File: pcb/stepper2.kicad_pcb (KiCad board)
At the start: 2 copper layers, 92 x 138 mm, 52 parts, among them J1 DA15_Receptacle_MountingHoles, J10 Conn_01x07_Pin, J11 FAN, J2 DA15_Receptacle_MountingHoles, J3 DA15_Receptacle_MountingHoles, J4 DE15_Receptacle_HighDensity, J5 DE15_Receptacle_HighDensity, J6 DE15_Receptacle_HighDensity, J7 Conn_01x04_Pin, J8 Conn_01x05_Pin, J9 Conn_01x06_Pin, SW1 SW_Push, SW2 SW_Push, SW3 SW_Push, SW4 SW_Push, SW5 SW_Push, SW6 SW_Push, U1 AM26LS32ACN, U2 AM26LS32Ax, U3 AM26LS32ACN, U4 TMC2226_BIGTREETECH, U5 TMC2209_BIGTREETECH, U6 TMC2209_BIGTREETECH

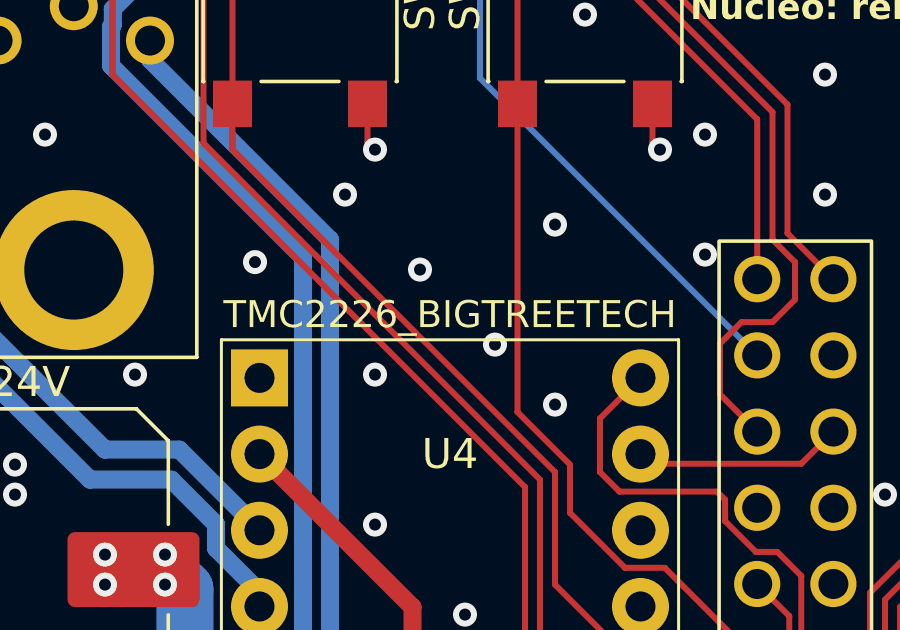
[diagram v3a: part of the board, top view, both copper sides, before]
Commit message: fixed mixed labeling for jog buttons; initial config of the NXT timers
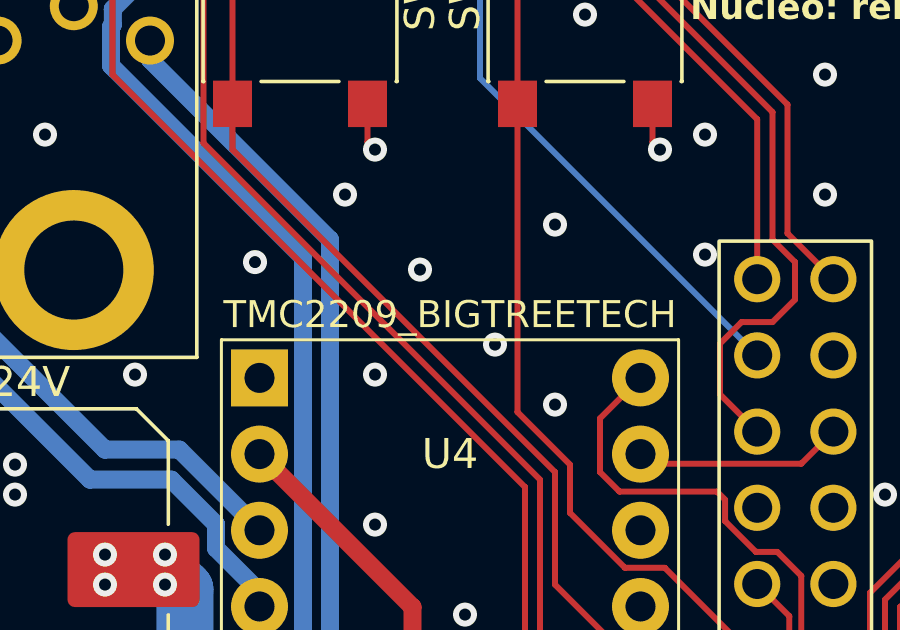
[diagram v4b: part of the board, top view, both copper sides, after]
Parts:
- U4: value TMC2226_BIGTREETECH -> TMC2209_BIGTREETECH
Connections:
- SW2 pad 1: UP2 -> DOWN3
- SW4 pad 1: DOWN1 -> DOWN2
- SW5 pad 1: DOWN2 -> UP2
- SW6 pad 1: DOWN3 -> DOWN1
- U10 pad B46: UP2 -> DOWN3
- U10 pad B50: DOWN3 -> DOWN1
- U10 pad B52: DOWN2 -> UP2
- U10 pad B54: DOWN1 -> DOWN2
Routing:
- net DOWN1: track 37.7 -> 56.2 mm
- net DOWN3: track 56.2 -> 41.5 mm
- net UP2: track 41.5 -> 31.9 mm, vias 0 -> 1
- net DOWN2: track 31.9 -> 37.7 mm, vias 1 -> 0

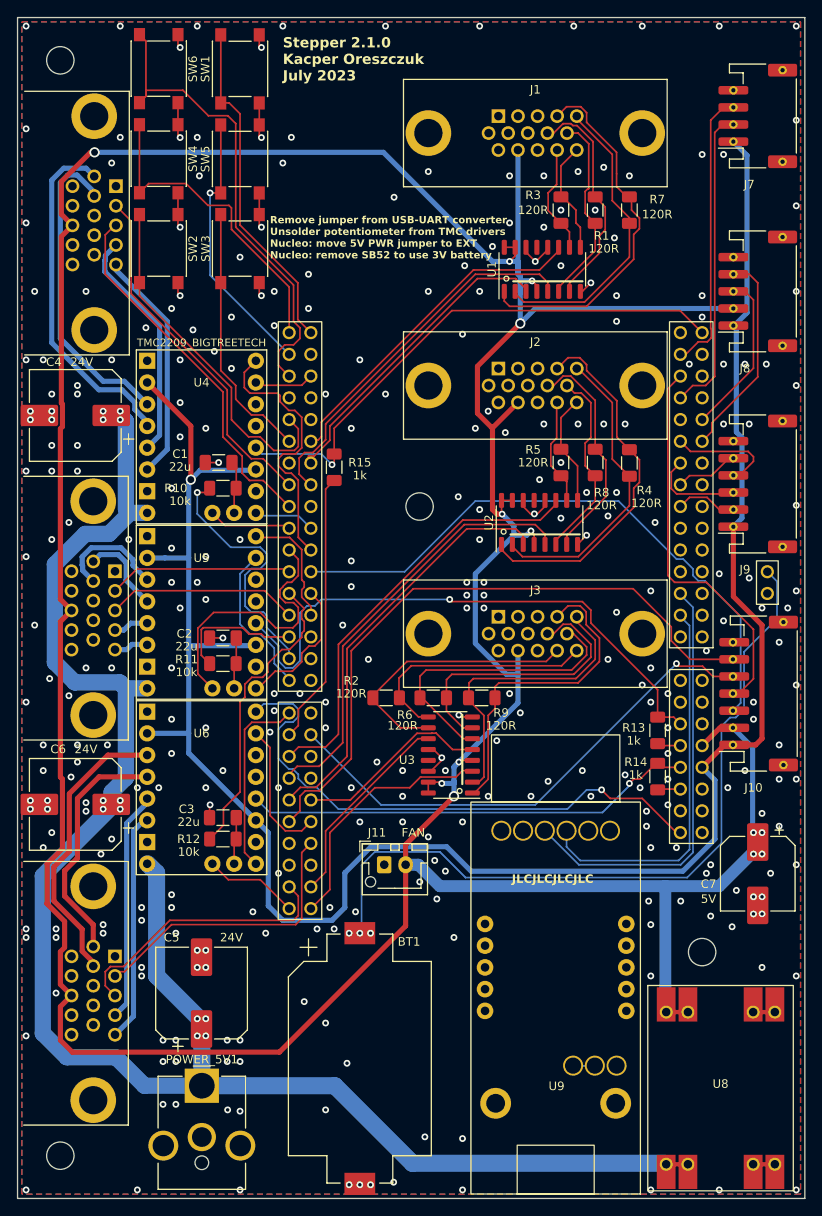
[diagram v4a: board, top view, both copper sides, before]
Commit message: PCB: NXT/DIR external output connectors and some polishing
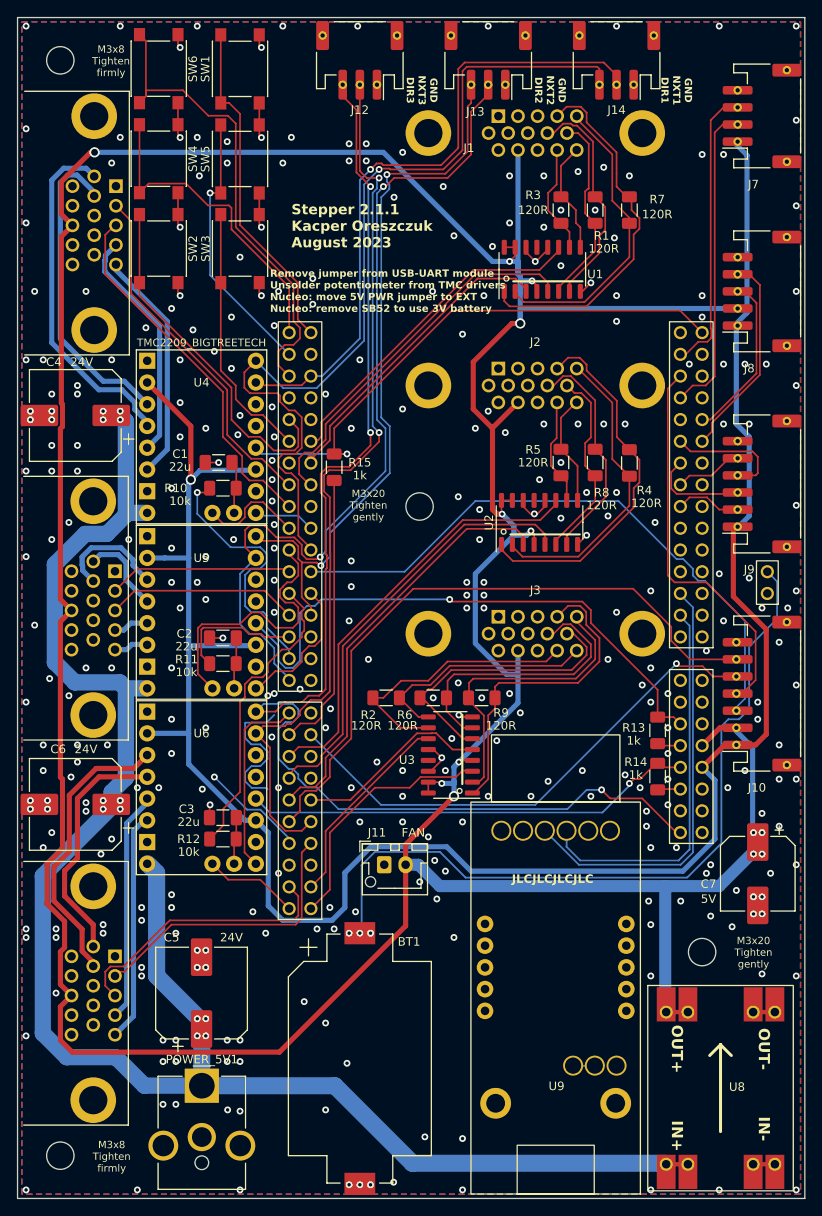
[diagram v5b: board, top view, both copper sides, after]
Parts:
- added J12: Conn_01x03_Pin, stepper2:JST_PH_S3B-PH-SM4-TB_1x03-1MP_P2.00mm_Horizontal, F.Cu at (40.0, 5.00)
- added J13: Conn_01x03_Pin, stepper2:JST_PH_S3B-PH-SM4-TB_1x03-1MP_P2.00mm_Horizontal, F.Cu at (55.0, 5.00)
- added J14: Conn_01x03_Pin, stepper2:JST_PH_S3B-PH-SM4-TB_1x03-1MP_P2.00mm_Horizontal, F.Cu at (70.0, 5.00)
- moved J7 0.50 mm to (87.0, 11.5)
- moved J8 0.50 mm to (87.0, 32.0)
- moved J9 0.50 mm to (87.0, 54.5)
- moved J10 0.40 mm to (87.0, 79.0)
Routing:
- net NXT3: track 16.2 -> 105.0 mm, vias 0 -> 2
- net DIR3: track 65.5 -> 151.2 mm, vias 1 -> 3
- net NXT2: track 18.2 -> 101.3 mm, vias 0 -> 2
- net DIR1: track 31.7 -> 106.9 mm, vias 0 -> 1
- net DIR2: track 14.4 -> 85.0 mm, vias 0 -> 2
- net NXT1: track 7.01 -> 76.2 mm, vias 0 -> 1
- net GND: track 43.4 -> 72.7 mm, vias 311 -> 332
- net DIAG1: track 9.71 -> 12.4 mm
- net +5V: track 458.4 -> 460.4 mm
- net EXTCOPI: track 12.9 -> 14.7 mm
- net +3V3: track 245.2 -> 246.8 mm
- net ENCB3+: track 35.0 -> 33.6 mm
- net ENCI3-: track 28.7 -> 27.3 mm
- net TMCUART1: track 63.8 -> 65.2 mm
- net TMCUARTTX1: track 31.9 -> 32.9 mm
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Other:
- board text added: "GND NXT1 DIR1"
- board text added: "GND NXT2 DIR2"
- board text added: "GND NXT3 DIR3"
- board text added: "M3x20 Tighten gently"
- board text added: "M3x8 Tighten firmly"
- board text added: "Remove jumper from USB-UART module Unsolder potentiometer from TMC drivers Nucleo: move 5V PWR jumper to EXT Nucleo: remove SB52 to use 3V battery"
- board text added: "Stepper 2.1.1 Kacper Oreszczuk August 2023"
- board text removed: "Remove jumper from USB-UART converter Unsolder potentiometer from TMC drivers Nucleo: move 5V PWR jumper to EXT Nucleo: remove SB52 to use 3V battery"
- board text removed: "Stepper 2.1.0 Kacper Oreszczuk July 2023"

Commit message: filtering capacitors for differential receivers; BOM and placement files for SMD elements
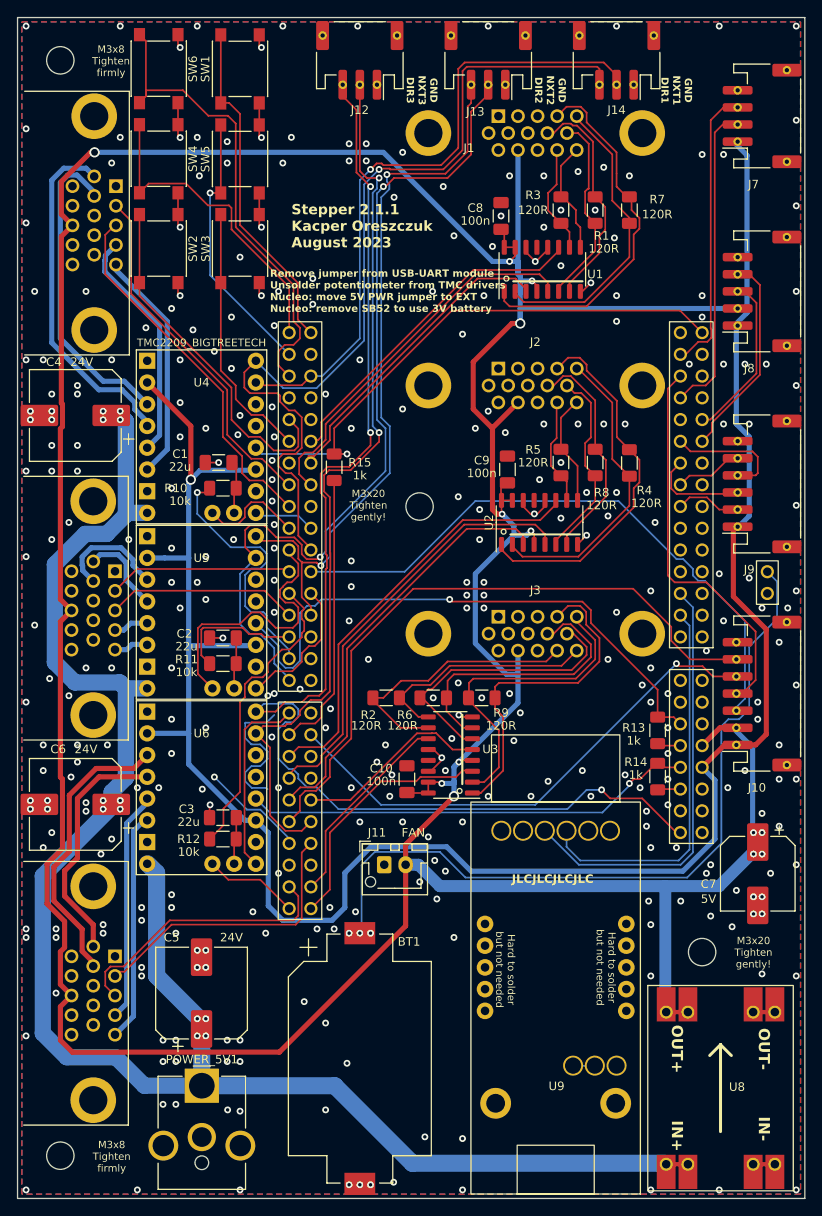
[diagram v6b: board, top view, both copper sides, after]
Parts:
- added C10: 100n, Capacitor_SMD:C_1206_3216Metric_Pad1.33x1.80mm_HandSolder, F.Cu at (45.5, 89.0)
- added C8: 100n, Capacitor_SMD:C_1206_3216Metric_Pad1.33x1.80mm_HandSolder, F.Cu at (56.5, 23.2)
- added C9: 100n, Capacitor_SMD:C_1206_3216Metric_Pad1.33x1.80mm_HandSolder, F.Cu at (57.2, 52.8)
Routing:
- net +5V: track 460.4 -> 467.5 mm
- net ENCA3+: track 35.1 -> 36.9 mm
- net ENCA3-: track 37.2 -> 38.4 mm
- net GND: vias 332 -> 333
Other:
- board text added: "Hard to solder but not needed"
- board text added: "M3x20 Tighten gently!"
- board text removed: "M3x20 Tighten gently"
